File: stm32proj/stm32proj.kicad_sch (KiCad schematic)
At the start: 10 parts, among them U1 STM32F103C8Tx

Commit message: schematics done
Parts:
- added C10, C11: 10p, symbol Device:C
- added C12, C13: 22u, symbol Device:C
- added C14, C9: 100n, symbol Device:C
- added D1: LED, symbol Device:LED
- added J1: USB_B_Micro, symbol Connector:USB_B_Micro
- added J2: Conn_01x04_Pin, symbol Connector:Conn_01x04_Pin
- added R1: 10k, symbol Device:R
- added R2, R3: 1k5, symbol Device:R
- added SW1: SW_SPDT, symbol Switch:SW_SPDT
- added U2: AMS1117-3.3, Package_TO_SOT_SMD:SOT-223-3_TabPin2, symbol Regulator_Linear:AMS1117-3.3
- added U3: AS5600, AS5600:SOIC8, symbol AS5600:AS5600
- added Y1: Crystal_GND24, symbol Device:Crystal_GND24
- C7, C8: value 10u -> 1u
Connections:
- net +3V3: now also C13.1, C14.1, D1.2 (A), J2.4 (Pin_4), R2.1, SW1.3 (C), U2.2 (VO), U3.1 (VDD5V), U3.2 (VDD3V3)
- net GND: now also C10.2, C11.2, C12.2, C13.2, C14.2, C9.2, J1.5 (GND), J2.1 (Pin_1), R3.2, SW1.1 (A), U2.1 (GND), U3.4 (GND), Y1.2 (G), Y1.4 (G)
- net S_OUT: now reaches U1.12 (PA2)
- net S_OUT: now also U3.3 (OUT)
- net DIR_CTRL: now reaches U1.13 (PA3)
- net DIR_CTRL: now also U3.8 (DIR)
- net PGO_CTRL: now reaches U1.14 (PA4)
- net PGO_CTRL: now also U3.5 (PGO)
- net SDA: now reaches U1.21 (PB10)
- net SDA: now also U3.7 (SCL)
- net SCL: now reaches U1.22 (PB11)
- net SCL: now also U3.6 (SDA)
- net USB_D-: now reaches U1.32 (PA11)
- net USB_D-: now also J1.2 (D-)
- net USB_D+: now reaches U1.33 (PA12)
- net USB_D+: now also J1.3 (D+), R2.2
- net SWDIO: now reaches U1.34 (PA13)
- net SWDIO: now also J2.3 (Pin_3)
- net SWCLK: now reaches U1.37 (PA14)
- net SWCLK: now also J2.2 (Pin_2)
- net BOOT: now reaches U1.44 (BOOT0)
- net BOOT: now also R1.2
- net HSE_IN: now reaches U1.5 (PD0)
- net HSE_IN: now also C10.1, Y1.1
- net HSE_OUT: now reaches U1.6 (PD1)
- net HSE_OUT: now also C11.1, Y1.3
- net NRST: now reaches U1.7 (NRST)
- net NRST: now also C9.1
- new net: R1.1, SW1.2 (B)
- new net PWR_LED: D1.1 (K), R3.1
- new net VBUS: C12.1, J1.1 (VBUS), U2.3 (VI)
- no-connect marks 0 -> 28
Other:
- note added: "AS5600 Sensor"
- note added: "Crystal"
- note added: "Debug"
- note added: "Decoupling/Noise Reduction"
- note added: "MCU"
- note added: "USB Setup"
- moved on the sheet: C1, C2, C3, C4, C5, C6, C7, C8, FB1, U1

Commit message: 3rd
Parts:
- removed FB1: FerriteBead, symbol Device:FerriteBead
- removed J1: USB_B_Micro, symbol Connector:USB_B_Micro
- removed SW1: SW_SPDT, symbol Switch:SW_SPDT
- added E1: LI0603G121R-10, LI0603G121R-10:FB_LI0603G121R-10, symbol LI0603G121R-10:LI0603G121R-10
- added J3: USB_C_Receptacle_USB2.0_14P, Connector_USB:USB_C_Receptacle_GCT_USB4105-xx-A_16P_TopMnt_Horizontal, symbol Connector:USB_C_Receptacle_USB2.0_14P
- added R4: 5k1, Resistor_SMD:R_0402_1005Metric, symbol Device:R
- added S1: TS09-63-25-R-260-SMT-TR, TS09-63-25-R-260-SMT-TR:SW_TS09-63-25-R-260-SMT-TR, symbol TS09-63-25-R-260-SMT-TR:TS09-63-25-R-260-SMT-TR
- C1, C10, C11, C14, C2, C3, C4, C5, C6, C7, C8, C9: footprint (none) -> Capacitor_SMD:C_0402_1005Metric
- C12, C13: footprint (none) -> Capacitor_SMD:C_0805_2012Metric
- D1: footprint (none) -> LED_SMD:LED_01005_0402Metric
- J2: footprint (none) -> Connector_PinHeader_1.00mm:PinHeader_1x04_P1.00mm_Vertical
- R1, R2, R3: footprint (none) -> Resistor_SMD:R_0402_1005Metric
- Y1: value Crystal_GND24 -> 8MHz; footprint (none) -> Crystal:Crystal_SMD_3225-4Pin_3.2x2.5mm
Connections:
- net +3.3VA: now also U1.12 (PA2), E1.1
- net +3V3: now also U1.42 (PB6), E1.2, S1.1
- net BOOT: now also S1.2
- net GND: now also R1.1, U1.43 (PB7), J3.A1 (GND), J3.A12 (GND), J3.B1 (GND), J3.B12 (GND), R4.2
- net HSE_IN: now also U1.46 (PB9); no longer U1.5 (PD0)
- net HSE_OUT: now also U1.2 (PC13); no longer U1.6 (PD1)
- net PGO_CTRL: now also U1.16 (PA6); no longer U1.14 (PA4)
- net SCL: now also U1.14 (PA4), U3.7 (SCL); no longer U1.22 (PB11), U3.6 (SDA)
- net SDA: now also U1.15 (PA5), U3.6 (SDA); no longer U1.21 (PB10), U3.7 (SCL)
- net SWDIO: now also U1.38 (PA15); no longer U1.34 (PA13)
- net S_OUT: now also U1.39 (PB3); no longer U1.12 (PA2)
- net VBUS: now also J3.A4 (VBUS), J3.A9 (VBUS), J3.B4 (VBUS), J3.B9 (VBUS)
- net USB_D+ renamed D+
- net D+: now also J3.A6 (D+), J3.B6 (D+)
- net USB_D- renamed D-
- net D-: now also J3.A7 (D-), J3.B7 (D-)
- new net CC: J3.A5 (CC1), J3.B5 (CC2), R4.1
- no-connect marks 28 -> 25
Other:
- moved on the sheet: R1, R2

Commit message: connection errors resolved
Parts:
- added J1: Conn_01x04_Pin, Connector_PinHeader_1.00mm:PinHeader_1x04_P1.00mm_Vertical, symbol Connector:Conn_01x04_Pin
- added R5: 4.7k, Resistor_SMD:R_0402_1005Metric, symbol Device:R
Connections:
- net +3V3: now also R5.1
- net TX: now reaches U1.10 (PA0)
- net TX: now also J1.3 (Pin_3)
- net RX: now reaches U1.11 (PA1)
- net RX: now also J1.4 (Pin_4)
- net U_SCL: now reaches U1.5 (PD0)
- net U_SCL: now also J1.1 (Pin_1)
- net U_SDA: now reaches U1.6 (PD1)
- net U_SDA: now also J1.2 (Pin_2), R5.2
- no-connect marks 25 -> 20
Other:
- note added: "I2C and UART"
- moved on the sheet: J2, R1

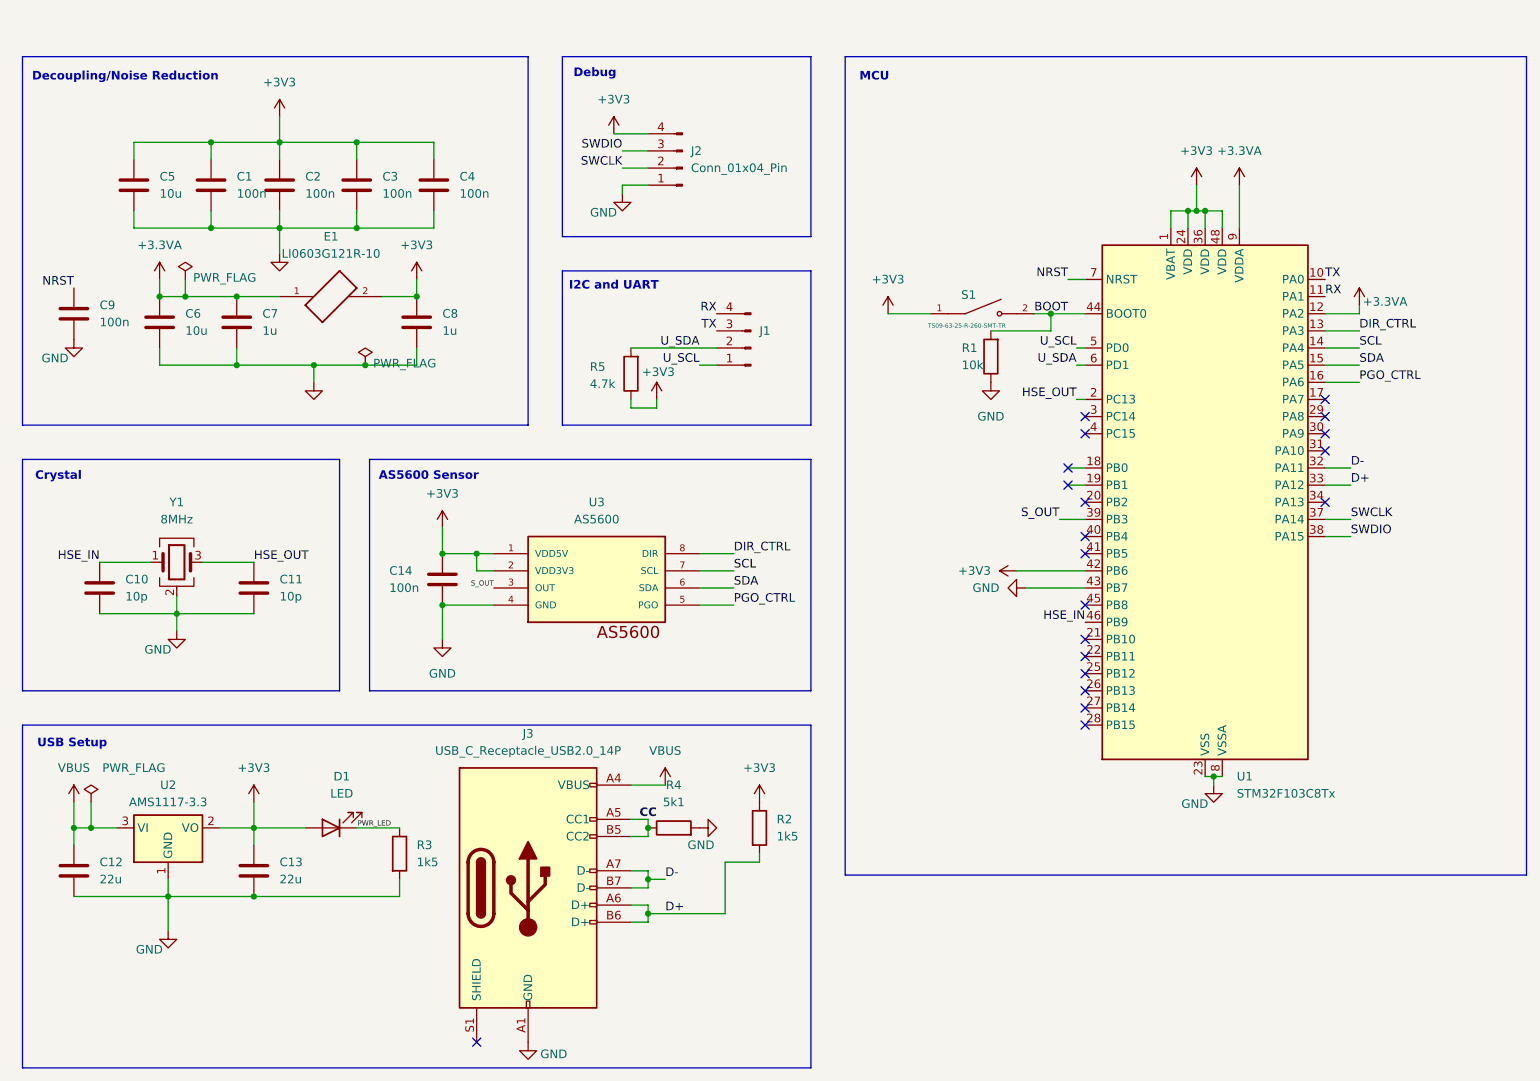
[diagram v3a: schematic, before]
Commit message: added mounting holes
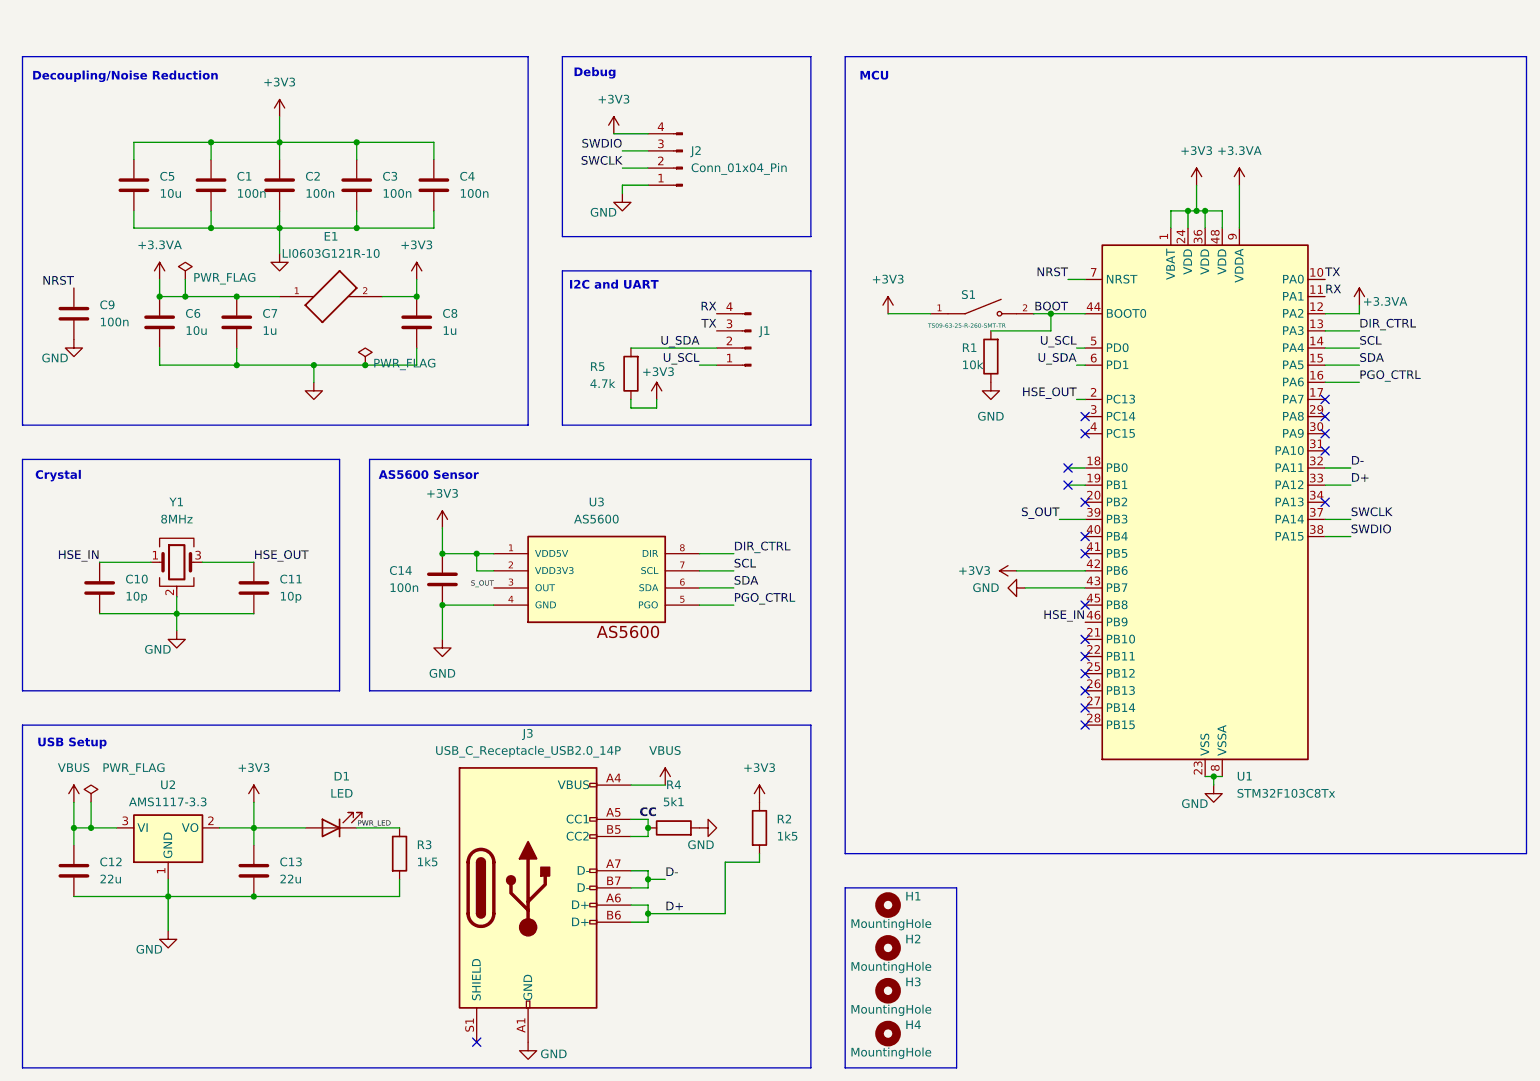
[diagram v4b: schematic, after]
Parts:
- added H1, H2, H3, H4: MountingHole, MountingHole:MountingHole_2.1mm, symbol Mechanical:MountingHole
